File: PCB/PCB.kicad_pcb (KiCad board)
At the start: 4 copper layers, 75 x 75 mm, 113 parts, among them J1 Conn_01x06_Female, J2 5054332681, U1 Hx711, U10 Hx711, U11 Hx711, U12 Hx711, U13 74HC165, U15 LT3042xMSE, U16 74HC165, U2 Hx711, U3 Hx711, U4 Hx711, U5 Hx711, U6 Hx711, U7 Hx711, U8 Hx711, U9 Hx711

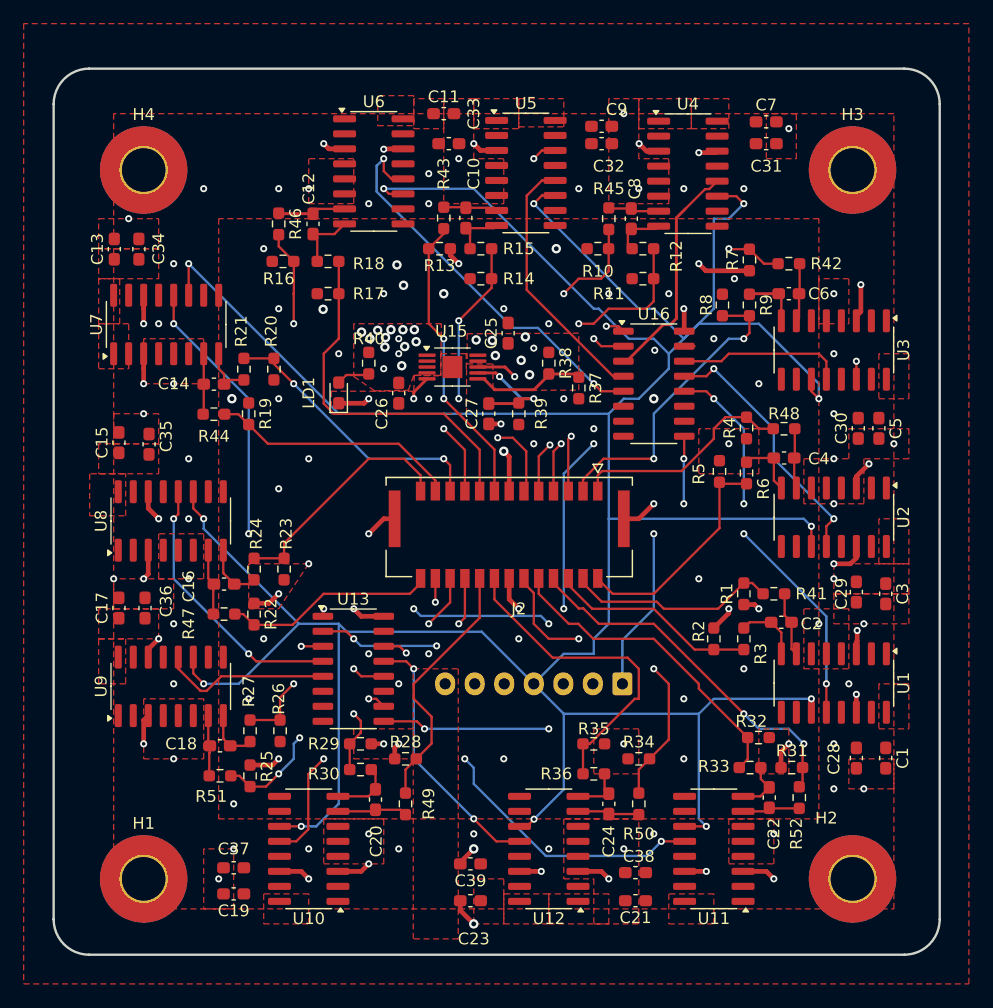
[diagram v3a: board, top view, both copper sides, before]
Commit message: PCB improvements made after conversing with Aila
Inner 5V boundary pour on the front layer has been replaced by four separate rectangle pours and the inner ground pour on the front plane has been replaced with individual separate ground pours for pads where possible, if impossible, using .4mm traces to ground vias.
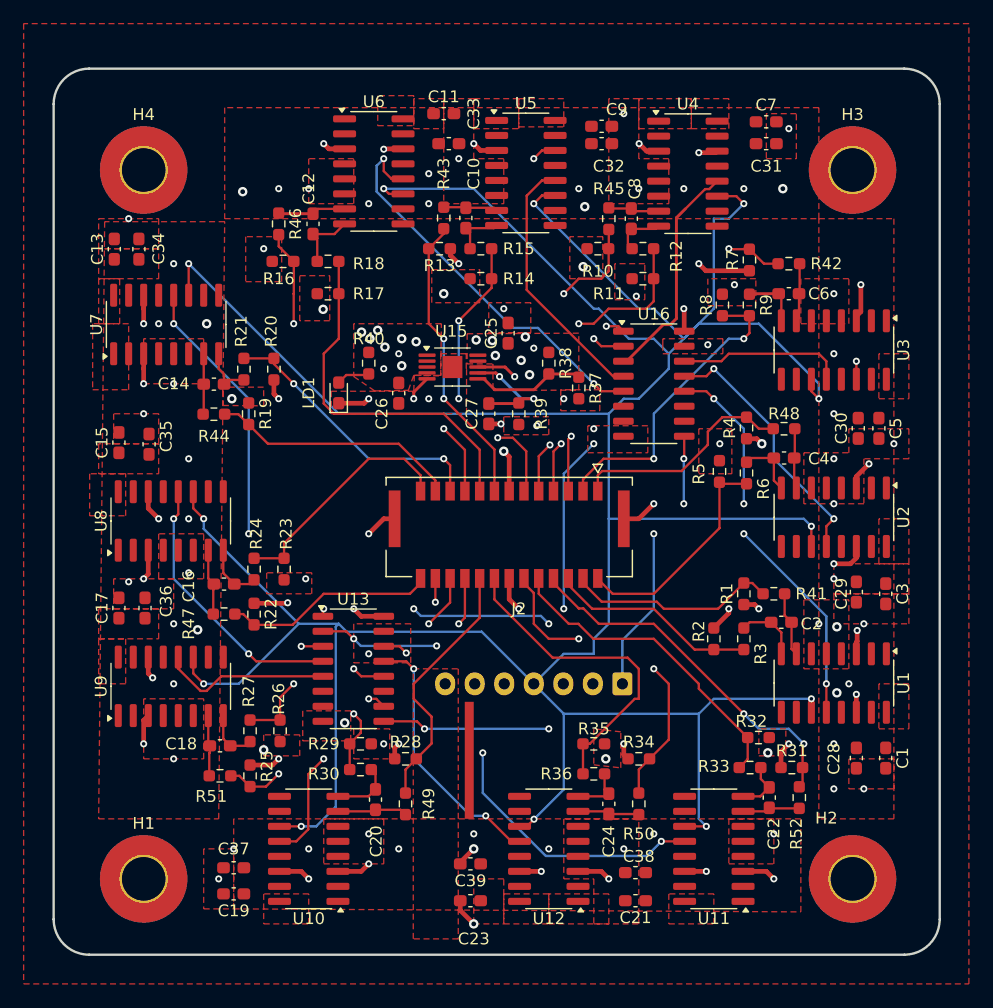
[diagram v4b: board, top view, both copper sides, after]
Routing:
- net GND: track 64.6 -> 68.4 mm, vias 89 -> 74
- net /DOUT5: track 37.1 -> 38.3 mm
- net /H4P: vias 3 -> 2
- net /H1P: vias 3 -> 2
- net /H9P: vias 3 -> 2

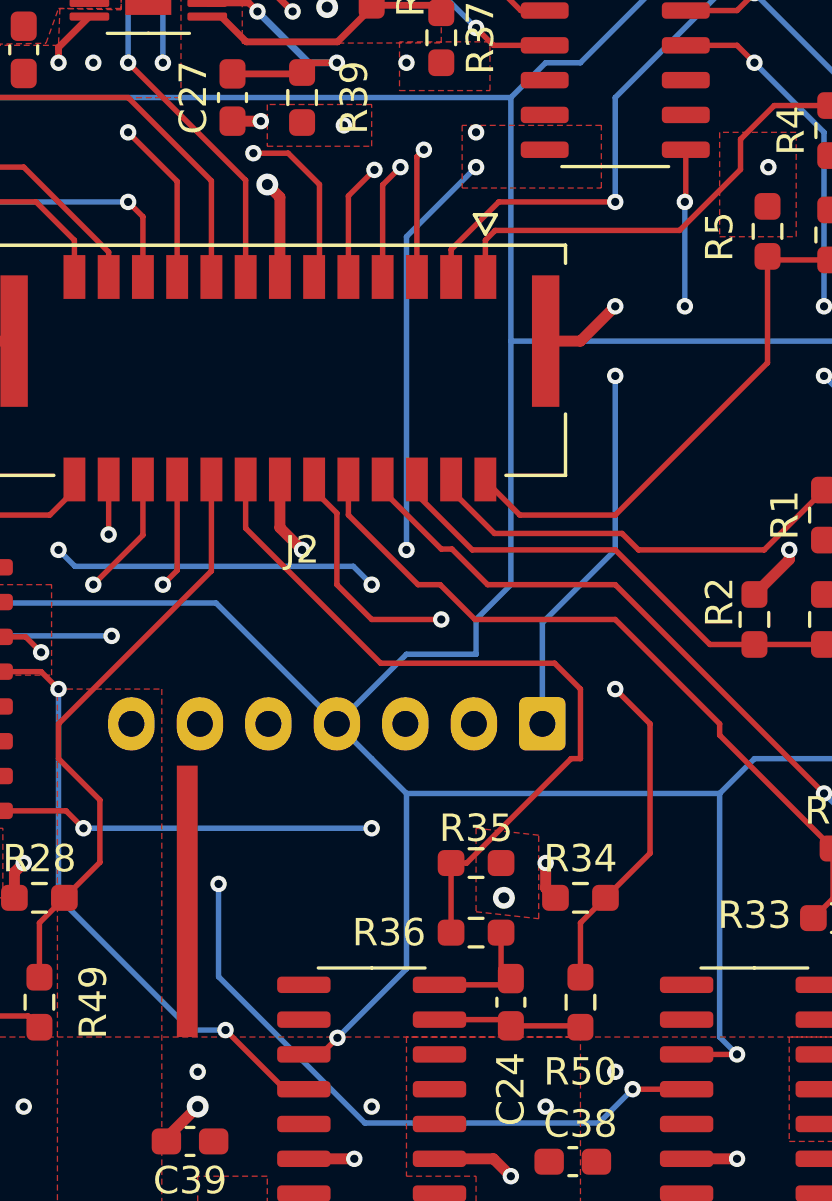
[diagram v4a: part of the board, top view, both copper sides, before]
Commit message: Updated 7 pin header pinout
Pinout has been adjusted to match the pinout of the flight computer.
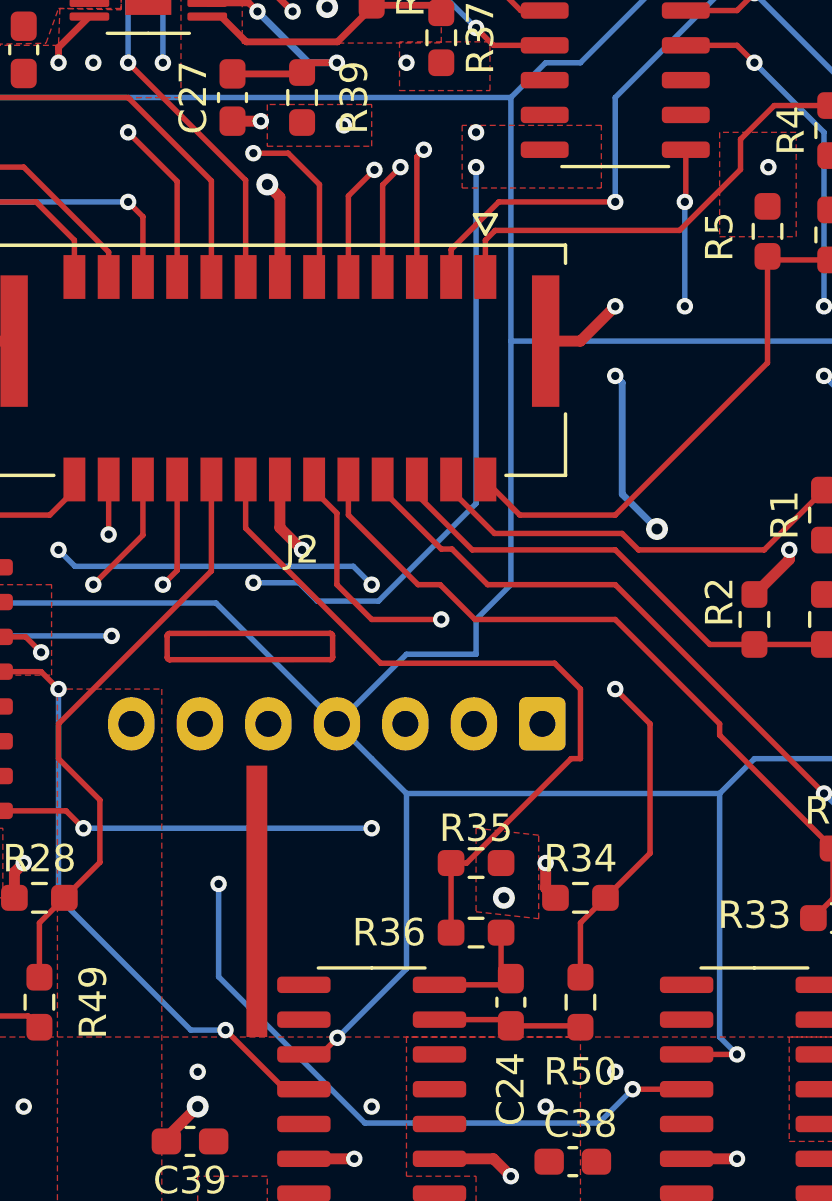
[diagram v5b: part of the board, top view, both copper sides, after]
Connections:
- J1 pad 1: /S_CLK -> GND
- J1 pad 3: /LOAD -> /S_CLK
- J1 pad 5: +5V -> /LOAD
- J1 pad 6: GND -> +3.3V
- J1 pad 7: +3.3V -> +5V
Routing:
- net /S_CLK: track 65.7 -> 64.2 mm, vias 4 -> 5
- net /LOAD: track 54.9 -> 55.4 mm
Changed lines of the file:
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@@
 			)
 		)
+		(property ki_fp_filters "Connector*:*_1x??_*")
+		(sheetname "Root")
+		(sheetfile "PCB.kicad_sch")
 		(attr through_hole)
 		(fp_line
@@
 			(remove_unused_layers no)
 			(roundrect_rratio 0.147059)
-			(net 29 "/S_CLK")
+			(net 1 "GND")
 			(pinfunction "Pin_1")
 			(pintype "passive")
@@
 			(layers "*.Cu" "*.Mask")
 			(remove_unused_layers no)
-			(net 31 "/LOAD")
+			(net 29 "/S_CLK")
 			(pinfunction "Pin_3")
 			(pintype "passive")
@@
 			(layers "*.Cu" "*.Mask")
 			(remove_unused_layers no)
-			(net 2 "+5V")
+			(net 31 "/LOAD")
 			(pinfunction "Pin_5")
 			(pintype "passive")
@@
 			(layers "*.Cu" "*.Mask")
 			(remove_unused_layers no)
-			(net 1 "GND")
+			(net 127 "+3.3V")
 			(pinfunction "Pin_6")
 			(pintype "passive")
@@
 			(layers "*.Cu" "*.Mask")
 			(remove_unused_layers no)
-			(net 127 "+3.3V")
+			(net 2 "+5V")
 			(pinfunction "Pin_7")
 			(pintype "passive")
@@
 	(gr_poly
 		(pts
-			(xy 243.078 147.32) (xy 243.84 147.32) (xy 243.84 137.414) (xy 243.078 137.414)
+			(xy 248.685541 132.588839) (xy 248.721589 132.603771) (xy 248.749179 132.631361) (xy 248.764111 132.667409)
+			(xy 248.766032 133.448918) (xy 248.764111 133.468427) (xy 248.749179 133.504475) (xy 248.721589 133.532065)
+			(xy 248.685541 133.546997) (xy 242.824032 133.548918) (xy 242.804523 133.546997) (xy 242.768475 133.532065)
+			(xy 242.740885 133.504475) (xy 242.725953 133.468427) (xy 242.724032 132.686918) (xy 242.725953 132.667409)
+			(xy 242.740885 132.631361) (xy 242.768475 132.603771) (xy 242.804523 132.588839) (xy 248.666032 132.586918)
+		)
+		(stroke
+			(width 0.2)
+			(type solid)
+		)
+		(fill none)
+		(layer "F.Cu")
+	)
+	(gr_poly
+		(pts
+			(xy 245.618 147.32) (xy 246.38 147.32) (xy 246.38 137.414) (xy 245.618 137.414)
 		)
 		(stroke
@@
 		(net 29)
 	)
+	(via
+		(at 260.604 128.778)
+		(size 0.8)
+		(drill 0.4)
+		(layers "F.Cu" "B.Cu")
+		(net 29)
+	)
+	(segment
+		(start 251.42 135.89)
+		(end 251.42 133.39)
+		(width 0.25)
+		(layer "In2.Cu")
+		(net 29)
+	)
 	(segment
 		(start 241.37 133.35)
-		(end 256.42 133.35)
+		(end 251.46 133.35)
 		(width 0.2)
 		(layer "In2.Cu")
@@
 	)
 	(segment
-		(start 256.42 133.35)
-		(end 256.42 135.89)
-		(width 0.2)
+		(start 251.46 133.35)
+		(end 256.032 133.35)
+		(width 0.25)
 		(layer "In2.Cu")
 		(net 29)
@@
 	)
 	(segment
+		(start 240.7 132.68)
+		(end 241.37 133.35)
+		(width 0.2)
+		(layer "In2.Cu")
+		(net 29)
+	)
+	(segment
 		(start 259.08 123.19)
 		(end 259.08 121.92)
@@
 	)
 	(segment
+		(start 251.42 133.39)
+		(end 251.46 133.35)
+		(width 0.25)
+		(layer "In2.Cu")
+		(net 29)
+	)
+	(segment
 		(start 257.21 121.32)
 		(end 252.73 116.84)
@@
 	)
 	(segment
-		(start 240.7 132.68)
-		(end 241.37 133.35)
-		(width 0.2)
+		(start 256.032 133.35)
+		(end 260.604 128.778)
+		(width 0.25)
 		(layer "In2.Cu")
 		(net 29)
@@
 	)
 	(segment
-		(start 240.7 132.68)
-		(end 234.28 132.68)
-		(width 0.2)
+		(start 259.334 127.508)
+		(end 260.604 128.778)
+		(width 0.25)
 		(layer "B.Cu")
 		(net 29)
 	)
 	(segment
-		(start 259.08 129.54)
-		(end 256.42 132.2)
+		(start 240.7 132.68)
+		(end 234.28 132.68)
 		(width 0.2)
 		(layer "B.Cu")
@@
 	(segment
 		(start 259.08 123.19)
-		(end 259.08 129.54)
-		(width 0.2)
+		(end 259.334 123.444)
+		(width 0.25)
 		(layer "B.Cu")
 		(net 29)
@@
 	)
 	(segment
-		(start 256.42 132.2)
-		(end 256.42 135.89)
-		(width 0.2)
+		(start 259.334 123.444)
+		(end 259.334 127.508)
+		(width 0.25)
 		(layer "B.Cu")
 		(net 29)
@@
 	)
 	(via
-		(at 251.46 129.54)
+		(at 245.872 130.74)
 		(size 0.6)
 		(drill 0.3)
@@
 	)
 	(segment
-		(start 251.42 135.89)
-		(end 251.42 129.58)
+		(start 245.272 130.14)
+		(end 231.74 130.14)
 		(width 0.2)
 		(layer "In1.Cu")
@@
 	)
 	(segment
-		(start 251.46 129.54)
-		(end 250.86 130.14)
-		(width 0.2)
+		(start 246.42 131.612)
+		(end 246.42 135.89)
+		(width 0.25)
 		(layer "In1.Cu")
 		(net 31)
 	)
 	(segment
-		(start 250.86 130.14)
-		(end 231.74 130.14)
-		(width 0.2)
+		(start 245.872 131.064)
+		(end 246.42 131.612)
+		(width 0.25)
 		(layer "In1.Cu")
 		(net 31)
 	)
 	(segment
-		(start 251.42 129.58)
-		(end 251.46 129.54)
+		(start 245.872 130.74)
+		(end 245.272 130.14)
 		(width 0.2)
 		(layer "In1.Cu")
@@
 	)
 	(segment
+		(start 245.872 130.74)
+		(end 245.872 131.064)
+		(width 0.25)
+		(layer "In1.Cu")
+		(net 31)
+	)
+	(segment
 		(start 255.057867 114.512133)
 		(end 255.057867 105.622133)
@@
 	)
 	(segment
-		(start 251.46 118.11)
+		(start 248.203062 131.41)
+		(end 250.438529 131.41)
+		(width 0.2)
+		(layer "B.Cu")
+		(net 31)
+	)
+	(segment
+		(start 254 127.848529)
 		(end 254 115.57)
 		(width 0.2)
@@
 	)
 	(segment
-		(start 251.46 129.54)
-		(end 251.46 118.11)
+		(start 250.438529 131.41)
+		(end 254 127.848529)
+		(width 0.2)
+		(layer "B.Cu")
+		(net 31)
+	)
+	(segment
+		(start 247.533062 130.74)
+		(end 248.203062 131.41)
+		(width 0.2)
+		(layer "B.Cu")
+		(net 31)
+	)
+	(segment
+		(start 245.872 130.74)
+		(end 247.533062 130.74)
 		(width 0.2)
 		(layer "B.Cu")

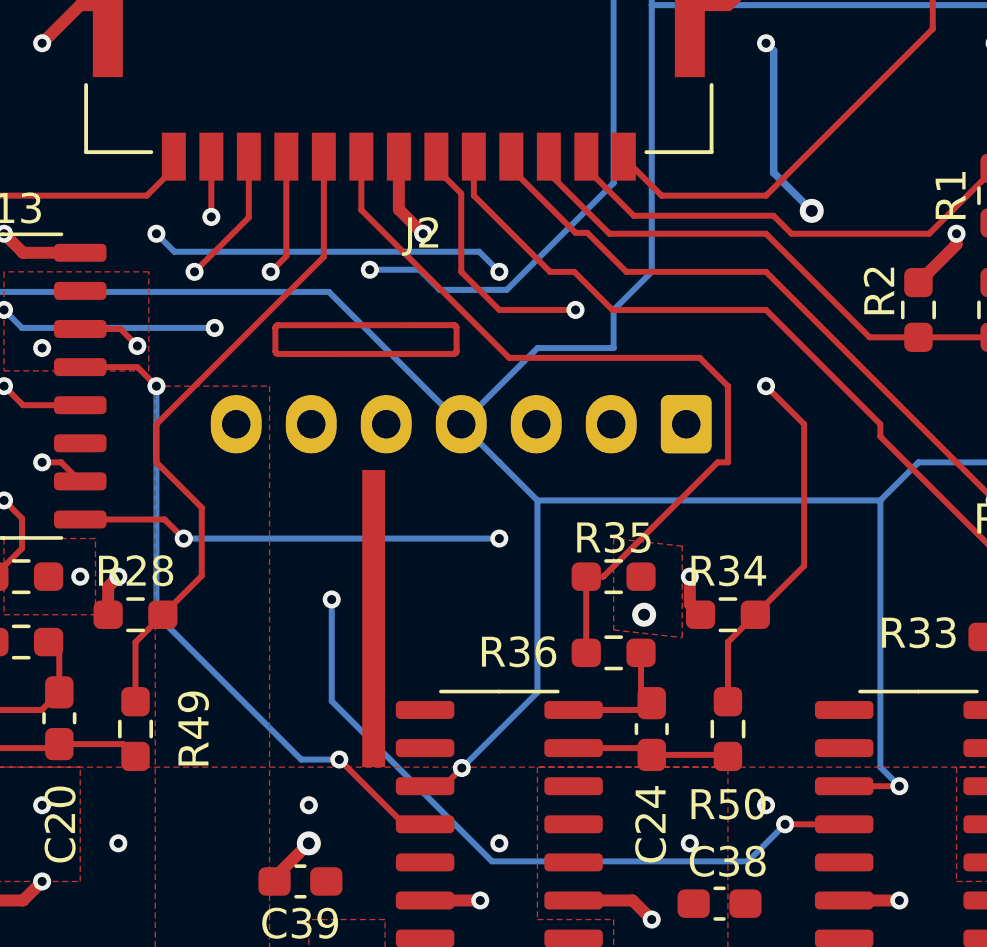
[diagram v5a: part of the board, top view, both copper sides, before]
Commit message: Rotated connector to better fit flight computer
Addition of a 3v3 zone expansion and passes drc.
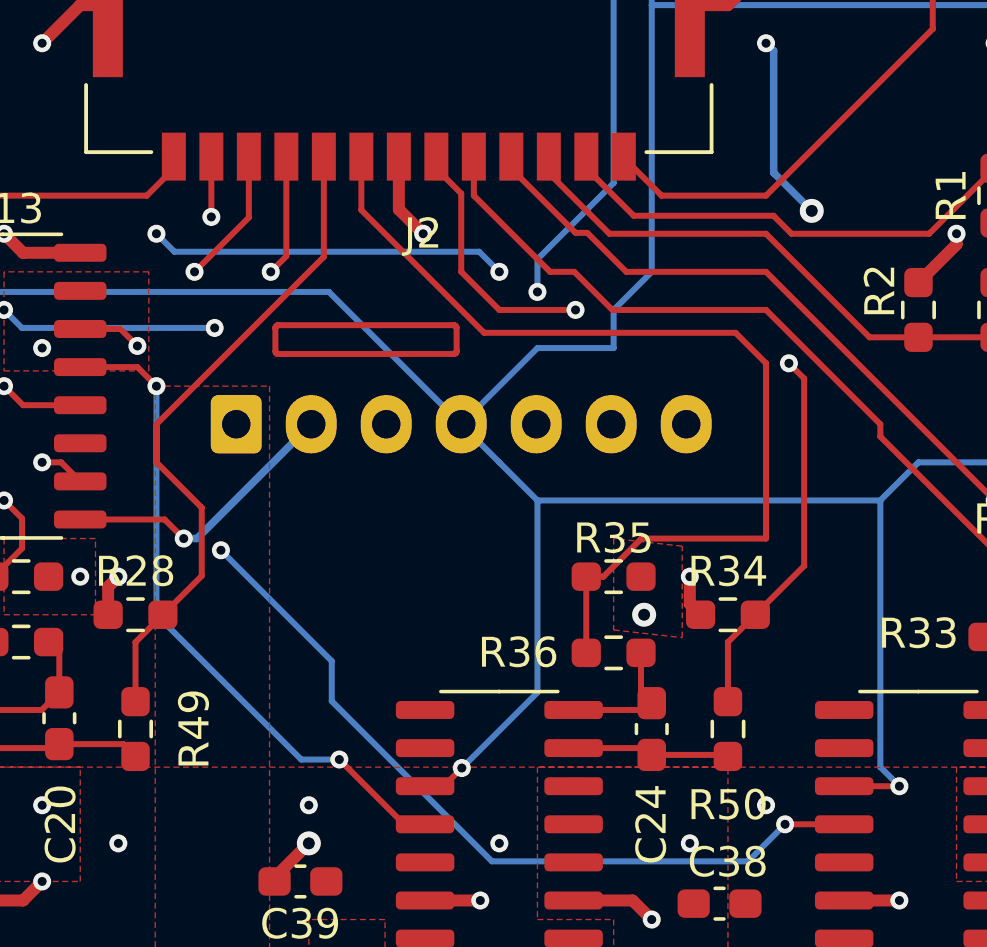
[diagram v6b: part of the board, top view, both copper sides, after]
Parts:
- moved J1 15.0 mm to (241.4, 135.9), turned to 0 degrees
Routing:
- net /DATA: track 19.6 -> 9.54 mm, vias 2 -> 1
- net /H14N: track 27.8 -> 32.3 mm
- net /DOUT5: track 38.3 -> 37.0 mm
- net /H14P: track 28.0 -> 28.9 mm
